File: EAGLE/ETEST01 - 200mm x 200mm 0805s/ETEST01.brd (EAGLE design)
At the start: 200 x 200 mm, 381 parts

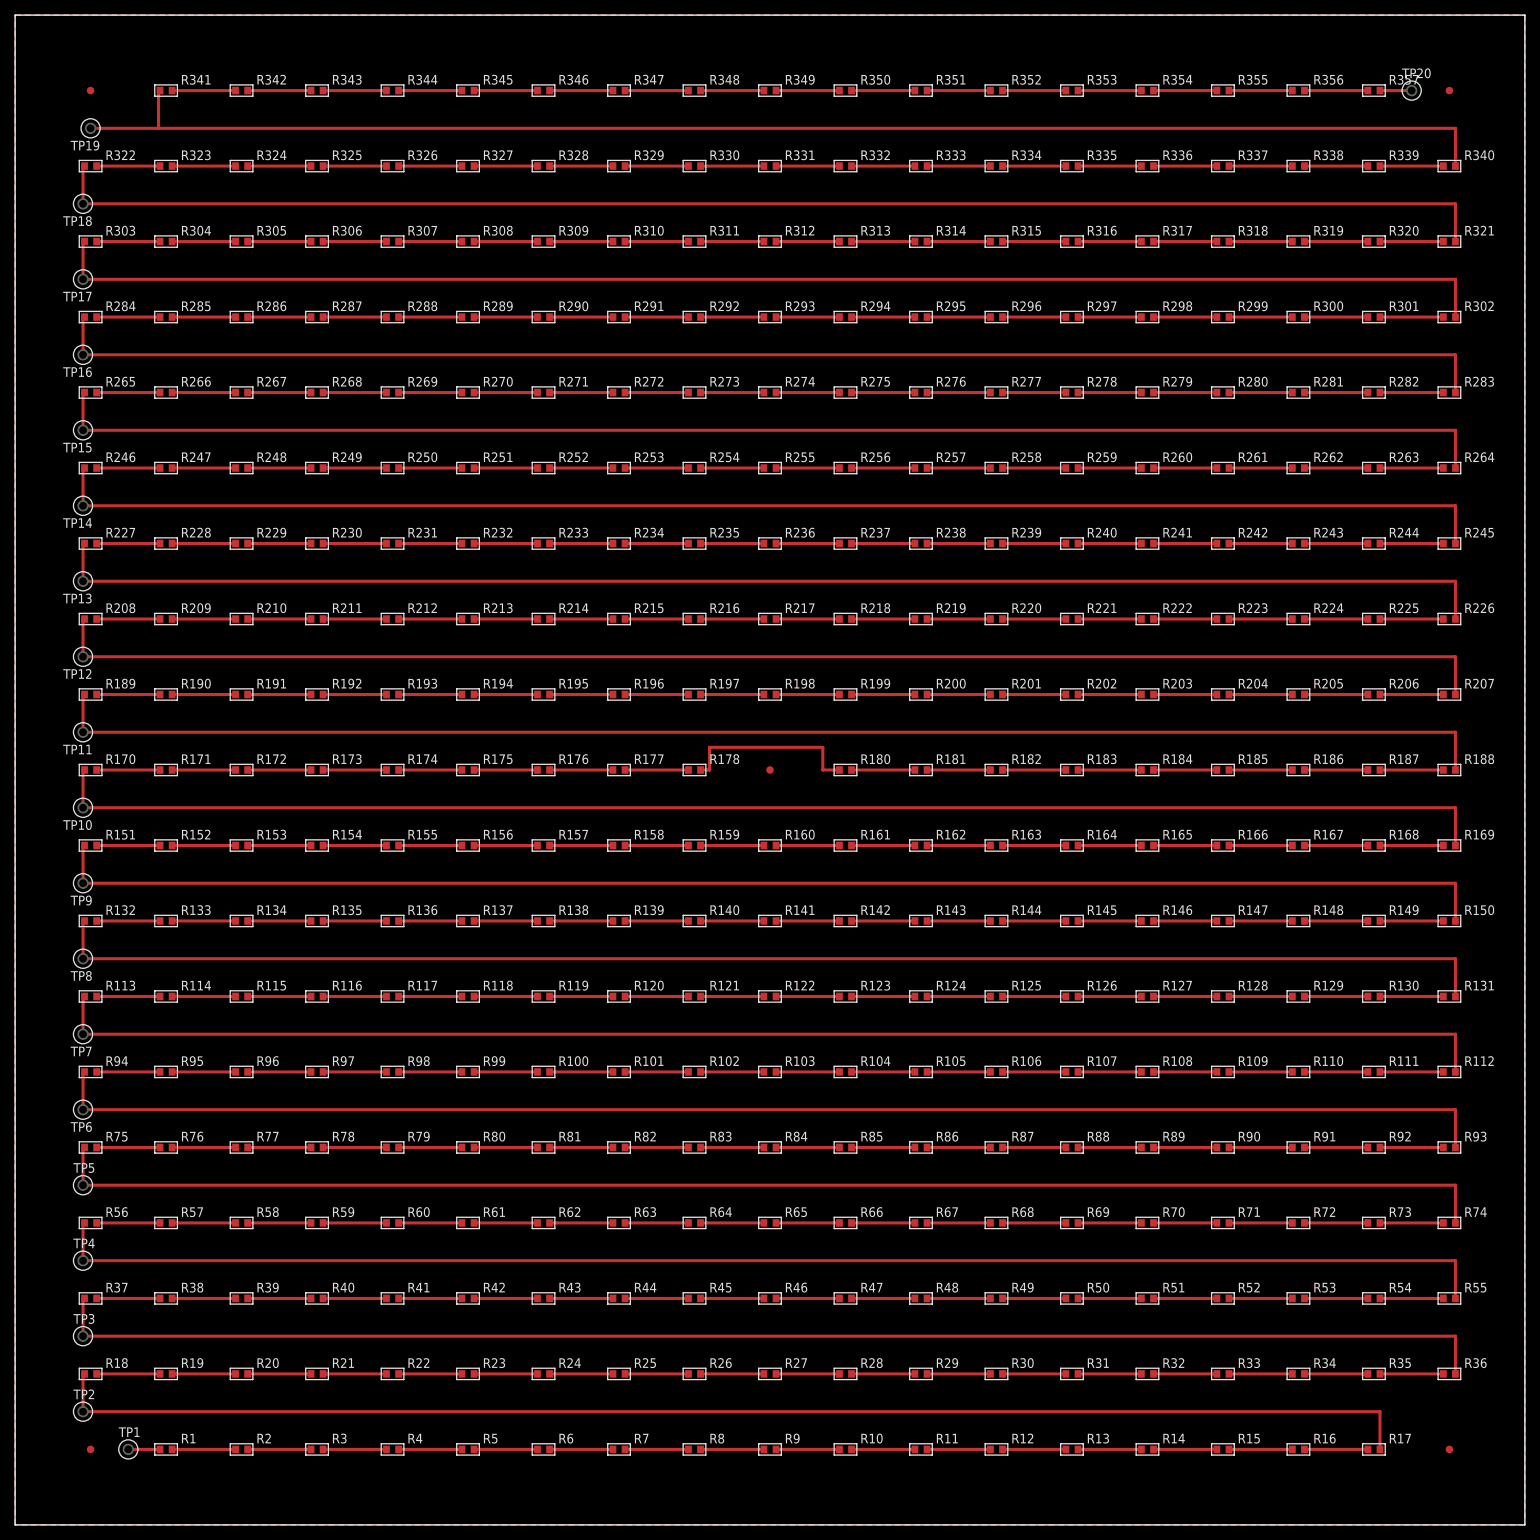
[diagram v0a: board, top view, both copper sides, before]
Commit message: Version 1 of ETEST01, these were the production files sent to fab, received 8/23/2015
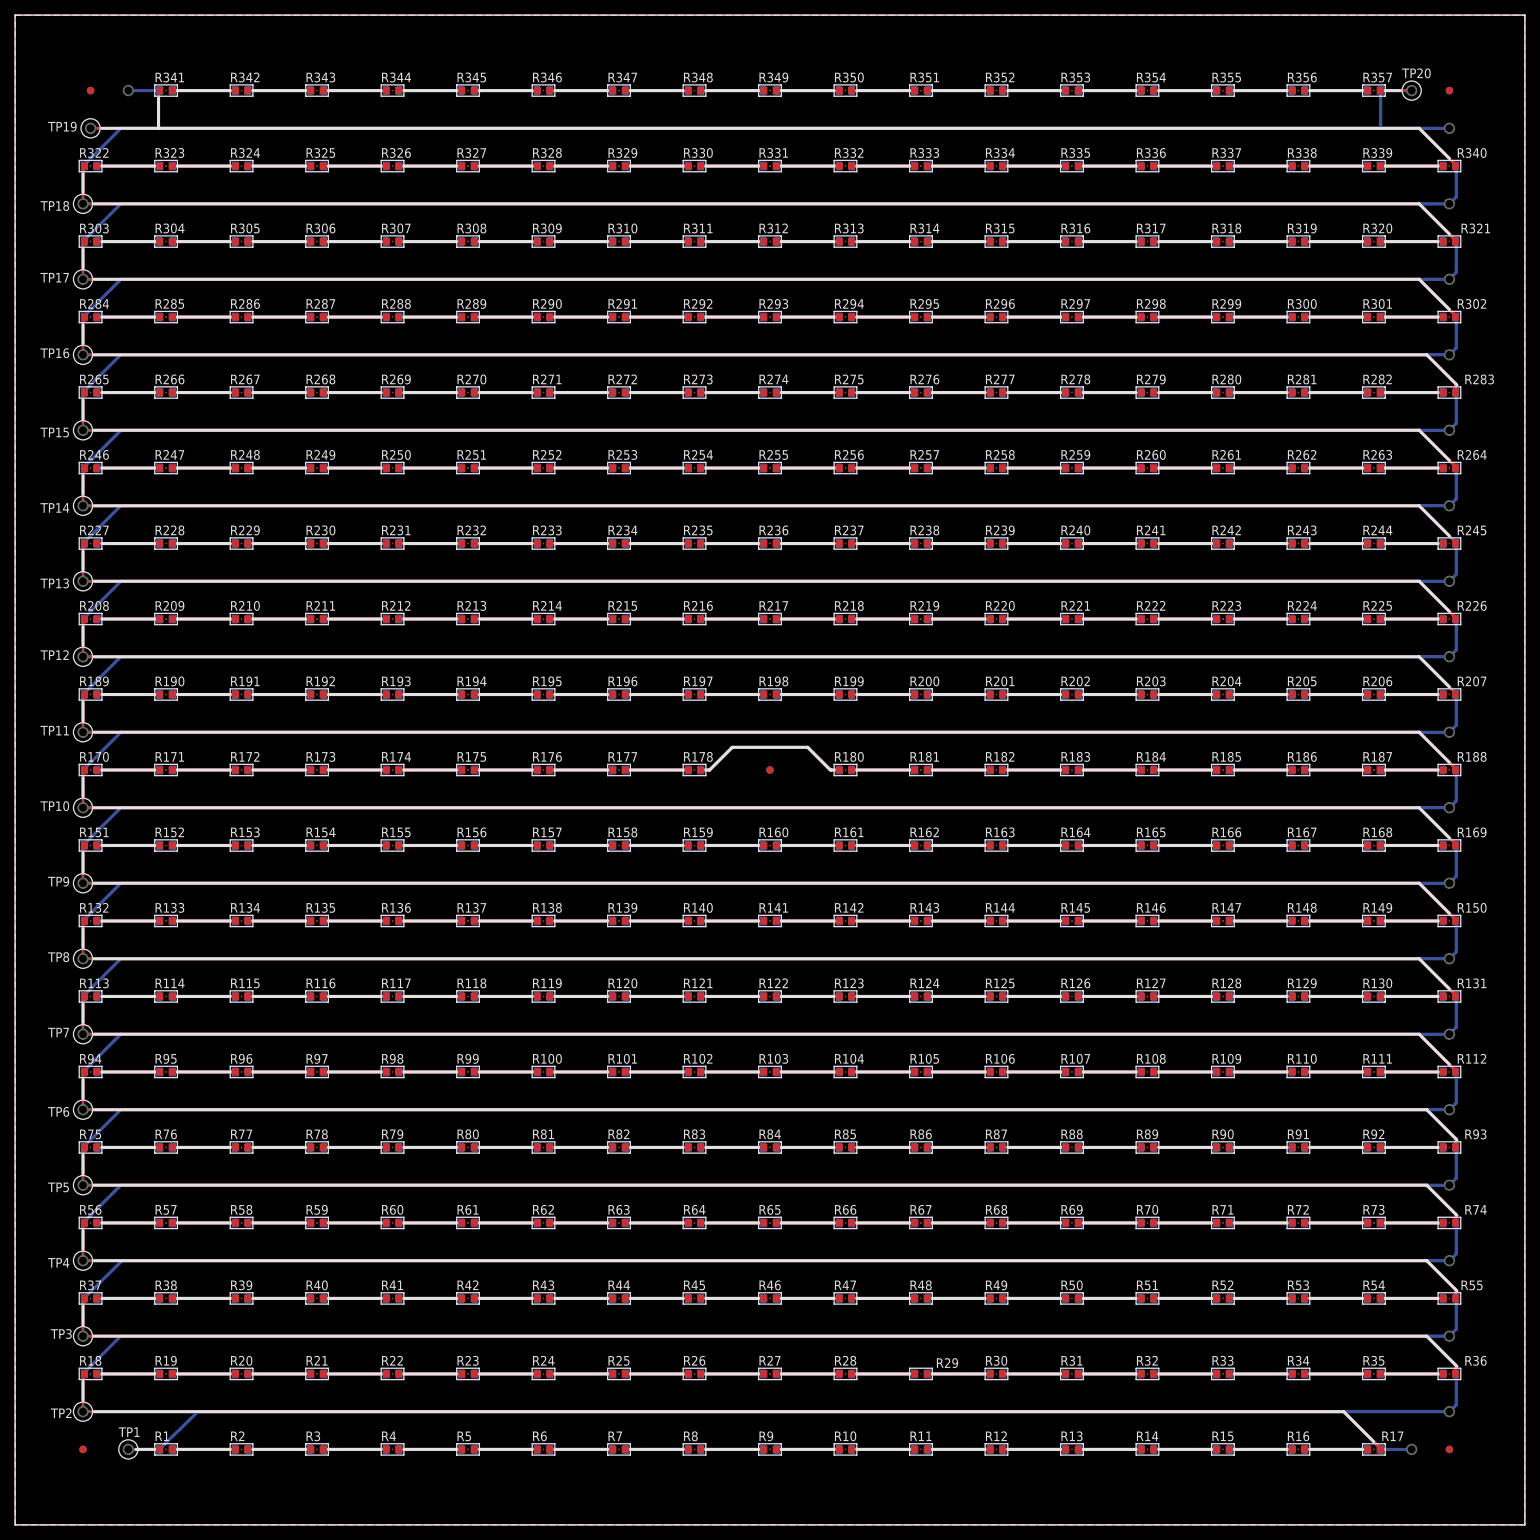
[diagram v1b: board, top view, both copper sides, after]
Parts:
- added FID10, FID6, FID7, FID8, FID9: FIDUCIAL, FirePick:FIDUCIAL
- added R179, R358, R359, R360, R361, R362, R363, R364, R365, R366, R367, R368, R369, R370, R371, R372, R373, R374, R375, R376, R377, R378, R379, R380, R381, R382, R383, R384, R385, R386, R387, R388, R389, R390, R391, R392, R393, R394, R395, R396, R397, R398, R399, R400, R401, R402, R403, R404, R405, R406, R407, R408, R409, R410, R411, R412, R413, R414, R415, R416, R417, R418, R419, R420, R421, R422, R423, R424, R425, R426, R427, R428, R429, R430, R431, R432, R433, R434, R435, R436, R437, R438, R439, R440, R441, R442, R443, R444, R445, R446, R447, R448, R449, R450, R451, R452, R453, R454, R455, R456, R457, R458, R459, R460, R461, R462, R463, R464, R465, R466, R467, R468, R469, R470, R471, R472, R473, R474, R475, R476, R477, R478, R479, R480, R481, R482, R483, R484, R485, R486, R487, R488, R489, R490, R491, R492, R493, R494, R495, R496, R497, R498, R499, R500, R501, R502, R503, R504, R505, R506, R507, R508, R509, R510, R511, R512, R513, R514, R515, R516, R517, R518, R519, R520, R521, R522, R523, R524, R525, R526, R527, R528, R529, R530, R531, R532, R533, R534, R535, R536, R537, R538, R539, R540, R541, R542, R543, R544, R545, R546, R547, R548, R549, R550, R551, R552, R553, R554, R555, R556, R557, R558, R559, R560, R561, R562, R563, R564, R565, R566, R567, R568, R569, R570, R571, R572, R573, R574, R575, R576, R577, R578, R579, R580, R581, R582, R583, R584, R585, R586, R587, R588, R589, R590, R591, R592, R593, R594, R595, R596, R597, R598, R599, R600, R601, R602, R603, R604, R605, R606, R607, R608, R609, R610, R611, R612, R613, R614, R615, R616, R617, R618, R619, R620, R621, R622, R623, R624, R625, R626, R627, R628, R629, R630, R631, R632, R633, R634, R635, R636, R637, R638, R639, R640, R641, R642, R643, R644, R645, R646, R647, R648, R649, R650, R651, R652, R653, R654, R655, R656, R657, R658, R659, R660, R661, R662, R663, R664, R665, R666, R667, R668, R669, R670, R671, R672, R673, R674, R675, R676, R677, R678, R679, R680, R681, R682, R683, R684, R685, R686, R687, R688, R689, R690, R691, R692, R693, R694, R695, R696, R697, R698, R699, R700, R701, R702, R703, R704, R705, R706, R707, R708, R709, R710, R711, R712: TESTPKG-RESISTOR0805, TinWhiskers:TESTPKG-R0805
- added TP21, TP22, TP23, TP24, TP25, TP26, TP27, TP28, TP29, TP30, TP31, TP32, TP33, TP34, TP35, TP36, TP37, TP38, TP39, TP40: CONN-TESTPOINT, FirePick:CON-TESTPOINT
- R1, R10, R100, R101, R102, R103, R104, R105, R106, R107, R108, R109, R11, R110, R111, R112, R113, R114, R115, R116, R117, R118, R119, R12, R120, R121, R122, R123, R124, R125, R126, R127, R128, R129, R13, R130, R131, R132, R133, R134, R135, R136, R137, R138, R139, R14, R140, R141, R142, R143, R144, R145, R146, R147, R148, R149, R15, R150, R151, R152, R153, R154, R155, R156, R157, R158, R159, R16, R160, R161, R162, R163, R164, R165, R166, R167, R168, R169, R17, R170, R171, R172, R173, R174, R175, R176, R177, R178, R18, R180, R181, R182, R183, R184, R185, R186, R187, R188, R189, R19, R190, R191, R192, R193, R194, R195, R196, R197, R198, R199, R2, R20, R200, R201, R202, R203, R204, R205, R206, R207, R208, R209, R21, R210, R211, R212, R213, R214, R215, R216, R217, R218, R219, R22, R220, R221, R222, R223, R224, R225, R226, R227, R228, R229, R23, R230, R231, R232, R233, R234, R235, R236, R237, R238, R239, R24, R240, R241, R242, R243, R244, R245, R246, R247, R248, R249, R25, R250, R251, R252, R253, R254, R255, R256, R257, R258, R259, R26, R260, R261, R262, R263, R264, R265, R266, R267, R268, R269, R27, R270, R271, R272, R273, R274, R275, R276, R277, R278, R279, R28, R280, R281, R282, R283, R284, R285, R286, R287, R288, R289, R290, R291, R292, R293, R294, R295, R296, R297, R298, R299, R3, R30, R300, R301, R302, R303, R304, R305, R306, R307, R308, R309, R31, R310, R311, R312, R313, R314, R315, R316, R317, R318, R319, R32, R320, R321, R322, R323, R324, R325, R326, R327, R328, R329, R33, R330, R331, R332, R333, R334, R335, R336, R337, R338, R339, R34, R340, R341, R342, R343, R344, R345, R346, R347, R348, R349, R35, R350, R351, R352, R353, R354, R355, R356, R357, R36, R37, R38, R39, R4, R40, R41, R42, R43, R44, R45, R46, R47, R48, R49, R5, R50, R51, R52, R53, R54, R55, R56, R57, R58, R59, R6, R60, R61, R62, R63, R64, R65, R66, R67, R68, R69, R7, R70, R71, R72, R73, R74, R75, R76, R77, R78, R79, R8, R80, R81, R82, R83, R84, R85, R86, R87, R88, R89, R9, R90, R91, R92, R93, R94, R95, R96, R97, R98, R99: value CPL-RES-0603-0-0.1W -> TESTPKG-RESISTOR0603; device TinWhiskers:R0603 -> TinWhiskers:TESTPKG-R0603
- moved FID1 1.00 mm to (-91.0, -90.0)
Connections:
- new net N$359: R584.2, R585.1
- new net N$360: R698.2, R699.1
- new net N$361: R699.2, R700.1
- new net N$362: R700.2, R701.1
- new net N$363: R701.2, R702.1
- new net N$364: R702.2, R703.1
- new net N$365: R703.2, R704.1
- new net N$366: R704.2, R705.1
- new net N$367: R705.2, R706.1
- new net N$368: R706.2, R707.1
- new net N$369: R707.2, R708.1
- new net N$370: R708.2, R709.1
- new net N$371: R709.2, R710.1
- new net N$372: R710.2, R711.1
- new net N$373: R711.2, R712.1
- new net N$374: R679.2, R680.1
- new net N$375: R680.2, R681.1
- new net N$376: R681.2, R682.1
- new net N$377: R682.2, R683.1
- new net N$378: R683.2, R684.1
- new net N$379: R684.2, R685.1
- new net N$380: R685.2, R686.1
- new net N$381: R686.2, R687.1
- new net N$382: R687.2, R688.1
- new net N$383: R688.2, R689.1
- new net N$384: R689.2, R690.1
- new net N$385: R690.2, R691.1
- new net N$386: R691.2, R692.1
- new net N$387: R692.2, R693.1
- new net N$388: R693.2, R694.1
- new net N$389: R694.2, R695.1
- new net N$390: R695.2, R696.1, TP39.1
- new net N$391: R697.2, R698.1
- new net N$392: R678.2, R679.1
- new net N$393: R661.2, R662.1
- new net N$394: R660.2, R661.1
- new net N$395: R662.2, R663.1
- new net N$396: R663.2, R664.1
- new net N$397: R664.2, R665.1
- new net N$398: R665.2, R666.1
- new net N$399: R666.2, R667.1
- new net N$400: R667.2, R668.1
- new net N$401: R668.2, R669.1
- new net N$402: R669.2, R670.1
- new net N$403: R670.2, R671.1
- new net N$404: R671.2, R672.1
- new net N$405: R672.2, R673.1
- new net N$406: R673.2, R674.1
- new net N$407: R674.2, R675.1
- new net N$408: R675.2, R676.1
- new net N$409: R676.2, R677.1, TP38.1
- new net N$410: R659.2, R660.1
- new net N$411: R640.2, R641.1
- new net N$412: R641.2, R642.1
- new net N$413: R642.2, R643.1
- new net N$414: R643.2, R644.1
- new net N$415: R644.2, R645.1
- new net N$416: R645.2, R646.1
- new net N$417: R646.2, R647.1
- new net N$418: R647.2, R648.1
- new net N$419: R648.2, R649.1
- new net N$420: R649.2, R650.1
- new net N$421: R650.2, R651.1
- new net N$422: R651.2, R652.1
- new net N$423: R652.2, R653.1
- new net N$424: R653.2, R654.1
- new net N$425: R654.2, R655.1
- new net N$426: R655.2, R656.1
- new net N$427: R656.2, R657.1
- new net N$428: R657.2, R658.1, TP37.1
- new net N$429: R622.2, R623.1
- new net N$430: R623.2, R624.1
- new net N$431: R624.2, R625.1
- new net N$432: R625.2, R626.1
- new net N$433: R626.2, R627.1
- new net N$434: R627.2, R628.1
- new net N$435: R628.2, R629.1
- new net N$436: R629.2, R630.1
- new net N$437: R630.2, R631.1
- new net N$438: R631.2, R632.1
- new net N$439: R632.2, R633.1
- new net N$440: R633.2, R634.1
- new net N$441: R634.2, R635.1
- new net N$442: R635.2, R636.1
- new net N$443: R636.2, R637.1
- new net N$444: R637.2, R638.1
- new net N$445: R638.2, R639.1, TP36.1
- new net N$446: R621.2, R622.1
- new net N$447: R619.2, R620.1, TP35.1
- new net N$448: R618.2, R619.1
- new net N$449: R617.2, R618.1
- new net N$450: R616.2, R617.1
- new net N$451: R615.2, R616.1
- new net N$452: R614.2, R615.1
- new net N$453: R613.2, R614.1
- new net N$454: R612.2, R613.1
- new net N$455: R611.2, R612.1
- new net N$456: R610.2, R611.1
- new net N$457: R609.2, R610.1
- new net N$458: R608.2, R609.1
- new net N$459: R607.2, R608.1
- new net N$460: R606.2, R607.1
- new net N$461: R605.2, R606.1
- new net N$462: R604.2, R605.1
- new net N$463: R603.2, R604.1
- new net N$464: R602.2, R603.1
- new net N$465: R600.2, R601.1, TP34.1
- new net N$466: R599.2, R600.1
- new net N$467: R598.2, R599.1
- new net N$468: R597.2, R598.1
- new net N$469: R596.2, R597.1
- new net N$470: R595.2, R596.1
- new net N$471: R594.2, R595.1
- new net N$472: R593.2, R594.1
- new net N$473: R592.2, R593.1
- new net N$474: R591.2, R592.1
- new net N$475: R590.2, R591.1
- new net N$476: R589.2, R590.1
- new net N$477: R588.2, R589.1
- new net N$478: R587.2, R588.1
- new net N$479: R586.2, R587.1
- new net N$480: R585.2, R586.1
- new net N$481: R583.2, R584.1
- new net N$482: R581.2, R582.1, TP33.1
- new net N$483: R580.2, R581.1
- new net N$484: R579.2, R580.1
- new net N$485: R578.2, R579.1
- new net N$486: R577.2, R578.1
- new net N$487: R576.2, R577.1
- new net N$488: R575.2, R576.1
- new net N$489: R574.2, R575.1
- new net N$490: R573.2, R574.1
- new net N$491: R572.2, R573.1
- new net N$492: R571.2, R572.1
- new net N$493: R570.2, R571.1
- new net N$494: R569.2, R570.1
- new net N$495: R568.2, R569.1
- new net N$496: R567.2, R568.1
- new net N$497: R566.2, R567.1
- new net N$498: R565.2, R566.1
- new net N$499: R564.2, R565.1
- new net N$500: R562.2, R563.1, TP32.1
- new net N$501: R561.2, R562.1
- new net N$502: R560.2, R561.1
- new net N$503: R559.2, R560.1
- new net N$504: R558.2, R559.1
- new net N$505: R557.2, R558.1
- new net N$506: R556.2, R557.1
- new net N$507: R555.2, R556.1
- new net N$508: R554.2, R555.1
- new net N$509: R553.2, R554.1
- new net N$510: R552.2, R553.1
- new net N$511: R551.2, R552.1
- new net N$512: R550.2, R551.1
- new net N$513: R549.2, R550.1
- new net N$514: R548.2, R549.1
- new net N$515: R547.2, R548.1
- new net N$516: R546.2, R547.1
- new net N$517: R545.2, R546.1
- new net N$518: R543.2, R544.1, TP31.1
- new net N$519: R542.2, R543.1
- new net N$520: R541.2, R542.1
- new net N$521: R540.2, R541.1
- new net N$522: R539.2, R540.1
- new net N$523: R538.2, R539.1
- new net N$524: R537.2, R538.1
- new net N$525: R536.2, R537.1
- new net N$526: R535.2, R536.1
- new net N$527: R533.2, R534.1
- new net N$528: R532.2, R533.1
- new net N$529: R531.2, R532.1
- new net N$530: R530.2, R531.1
- new net N$531: R529.2, R530.1
- new net N$532: R528.2, R529.1
- new net N$533: R527.2, R528.1
- new net N$534: R525.2, R526.1, TP30.1
- new net N$535: R524.2, R525.1
- new net N$536: R523.2, R524.1
- new net N$537: R522.2, R523.1
- new net N$538: R521.2, R522.1
- new net N$539: R520.2, R521.1
- new net N$540: R519.2, R520.1
- new net N$541: R518.2, R519.1
- new net N$542: R517.2, R518.1
- new net N$543: R516.2, R517.1
- new net N$544: R515.2, R516.1
- new net N$545: R514.2, R515.1
- new net N$546: R513.2, R514.1
- new net N$547: R512.2, R513.1
- new net N$548: R511.2, R512.1
- new net N$549: R510.2, R511.1
- new net N$550: R509.2, R510.1
- new net N$551: R508.2, R509.1
- new net N$552: R506.2, R507.1, TP29.1
- new net N$553: R505.2, R506.1
- new net N$554: R504.2, R505.1
- new net N$555: R503.2, R504.1
- new net N$556: R502.2, R503.1
- new net N$557: R501.2, R502.1
- new net N$558: R500.2, R501.1
- new net N$559: R499.2, R500.1
- new net N$560: R498.2, R499.1
- new net N$561: R497.2, R498.1
- new net N$562: R496.2, R497.1
- new net N$563: R495.2, R496.1
- new net N$564: R494.2, R495.1
- new net N$565: R493.2, R494.1
- new net N$566: R492.2, R493.1
- new net N$567: R491.2, R492.1
- new net N$568: R490.2, R491.1
- new net N$569: R489.2, R490.1
- new net N$570: R487.2, R488.1, TP28.1
- new net N$571: R486.2, R487.1
- new net N$572: R485.2, R486.1
- new net N$573: R484.2, R485.1
- new net N$574: R483.2, R484.1
- new net N$575: R482.2, R483.1
- new net N$576: R481.2, R482.1
- new net N$577: R480.2, R481.1
- new net N$578: R479.2, R480.1
- new net N$579: R478.2, R479.1
- new net N$580: R477.2, R478.1
- new net N$581: R476.2, R477.1
- new net N$582: R475.2, R476.1
- new net N$583: R474.2, R475.1
- new net N$584: R473.2, R474.1
- new net N$585: R472.2, R473.1
- new net N$586: R471.2, R472.1
- new net N$587: R470.2, R471.1
- new net N$588: R468.2, R469.1, TP27.1
- new net N$589: R467.2, R468.1
- new net N$590: R466.2, R467.1
- new net N$591: R465.2, R466.1
- new net N$592: R464.2, R465.1
- new net N$593: R463.2, R464.1
- new net N$594: R462.2, R463.1
- new net N$595: R461.2, R462.1
- new net N$596: R460.2, R461.1
- new net N$597: R459.2, R460.1
- new net N$598: R458.2, R459.1
- new net N$599: R457.2, R458.1
- new net N$600: R456.2, R457.1
- new net N$601: R455.2, R456.1
- new net N$602: R454.2, R455.1
- new net N$603: R453.2, R454.1
- new net N$604: R452.2, R453.1
- new net N$605: R451.2, R452.1
- new net N$606: R449.2, R450.1, TP26.1
- new net N$607: R448.2, R449.1
- new net N$608: R447.2, R448.1
- new net N$609: R446.2, R447.1
- new net N$610: R445.2, R446.1
- new net N$611: R444.2, R445.1
- new net N$612: R443.2, R444.1
- new net N$613: R442.2, R443.1
- new net N$614: R441.2, R442.1
- new net N$615: R440.2, R441.1
- new net N$616: R439.2, R440.1
- new net N$617: R438.2, R439.1
- new net N$618: R437.2, R438.1
- new net N$619: R436.2, R437.1
- new net N$620: R435.2, R436.1
- new net N$621: R434.2, R435.1
- new net N$622: R433.2, R434.1
- new net N$623: R432.2, R433.1
- new net N$624: R429.2, R430.1
- new net N$625: R428.2, R429.1
- new net N$626: R427.2, R428.1
- new net N$627: R426.2, R427.1
- new net N$628: R425.2, R426.1
- new net N$629: R424.2, R425.1
- new net N$630: R423.2, R424.1
- new net N$631: R422.2, R423.1
- new net N$632: R421.2, R422.1
- new net N$633: R420.2, R421.1
- new net N$634: R419.2, R420.1
- new net N$635: R418.2, R419.1
- new net N$636: R417.2, R418.1
- new net N$637: R416.2, R417.1
- new net N$638: R415.2, R416.1
- new net N$639: R414.2, R415.1
- new net N$640: R413.2, R414.1
- new net N$641: R410.2, R411.1
- new net N$642: R409.2, R410.1
- new net N$643: R408.2, R409.1
- new net N$644: R407.2, R408.1
- new net N$645: R406.2, R407.1
- new net N$646: R405.2, R406.1
- new net N$647: R404.2, R405.1
- new net N$648: R403.2, R404.1
- new net N$649: R402.2, R403.1
- new net N$650: R401.2, R402.1
- new net N$651: R400.2, R401.1
- new net N$652: R399.2, R400.1
- new net N$653: R398.2, R399.1
- new net N$654: R397.2, R398.1
- new net N$655: R396.2, R397.1
- new net N$656: R395.2, R396.1
- new net N$657: R394.2, R395.1
- new net N$658: R391.2, R392.1
- new net N$659: R390.2, R391.1
- new net N$660: R389.2, R390.1
- new net N$661: R388.2, R389.1
- new net N$662: R387.2, R388.1
- new net N$663: R386.2, R387.1
- new net N$664: R385.2, R386.1
- new net N$665: R384.2, R385.1
- new net N$666: R383.2, R384.1
- new net N$667: R382.2, R383.1
- new net N$668: R381.2, R382.1
- new net N$669: R380.2, R381.1
- new net N$670: R379.2, R380.1
- new net N$671: R378.2, R379.1
- new net N$672: R377.2, R378.1
- new net N$673: R376.2, R377.1
- new net N$674: R375.2, R376.1
- new net N$675: R372.2, R373.1
- new net N$676: R371.2, R372.1
- new net N$677: R370.2, R371.1
- new net N$678: R369.2, R370.1
- new net N$679: R368.2, R369.1
- new net N$680: R367.2, R368.1
- new net N$681: R366.2, R367.1
- new net N$682: R365.2, R366.1
- new net N$683: R364.2, R365.1
- new net N$684: R363.2, R364.1
- new net N$685: R362.2, R363.1
- new net N$686: R361.2, R362.1
- new net N$687: R360.2, R361.1
- new net N$688: R359.2, R360.1
- new net N$689: R358.2, R359.1
- new net N$690: R179.2, R358.1
- new net N$691: R374.2, R375.1
- new net N$692: R393.2, R394.1
- new net N$693: R412.2, R413.1
- new net N$694: R431.2, R432.1
- new net N$695: R450.2, R451.1
- new net N$696: R469.2, R470.1
- new net N$697: R488.2, R489.1
- new net N$698: R507.2, R508.1
- new net N$699: R526.2, R527.1
- new net N$700: R544.2, R545.1
- new net N$701: R563.2, R564.1
- new net N$702: R582.2, R583.1
- new net N$703: R601.2, R602.1
- new net N$704: R620.2, R621.1
- new net N$705: R639.2, R640.1
- new net N$706: R658.2, R659.1
- new net N$707: R677.2, R678.1
- new net N$708: R696.2, R697.1
- new net N$709: R430.2, R431.1, TP25.1
- new net N$710: R411.2, R412.1, TP24.1
- new net N$711: R392.2, R393.1, TP23.1
- new net N$712: R373.2, R374.1, TP22.1
- new net N$713: R534.2, R535.1
- new net N$714: R712.2, TP40.1
- new net N$715: R179.1, TP21.1
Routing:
- net N$711: track 0.00 -> 188.4 mm
- net N$709: track 0.00 -> 188.4 mm
- net N$606: track 0.00 -> 188.4 mm
- net N$588: track 0.00 -> 188.4 mm
- net N$570: track 0.00 -> 188.4 mm
- net N$552: track 0.00 -> 188.4 mm
- net N$534: track 0.00 -> 188.4 mm
- net N$518: track 0.00 -> 188.4 mm
- net N$500: track 0.00 -> 188.4 mm
- net N$482: track 0.00 -> 188.4 mm
- net N$465: track 0.00 -> 188.4 mm
- net N$447: track 0.00 -> 188.4 mm
- net N$445: track 0.00 -> 188.4 mm
- net N$428: track 0.00 -> 188.4 mm
- net N$409: track 0.00 -> 188.4 mm
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- added copper zone on layer 16, net N$716
